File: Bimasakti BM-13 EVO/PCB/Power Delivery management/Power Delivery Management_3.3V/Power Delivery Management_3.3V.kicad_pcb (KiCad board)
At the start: 2 copper layers, 35 x 43 mm, 25 parts, among them J1 +12V In, J2 3.3V

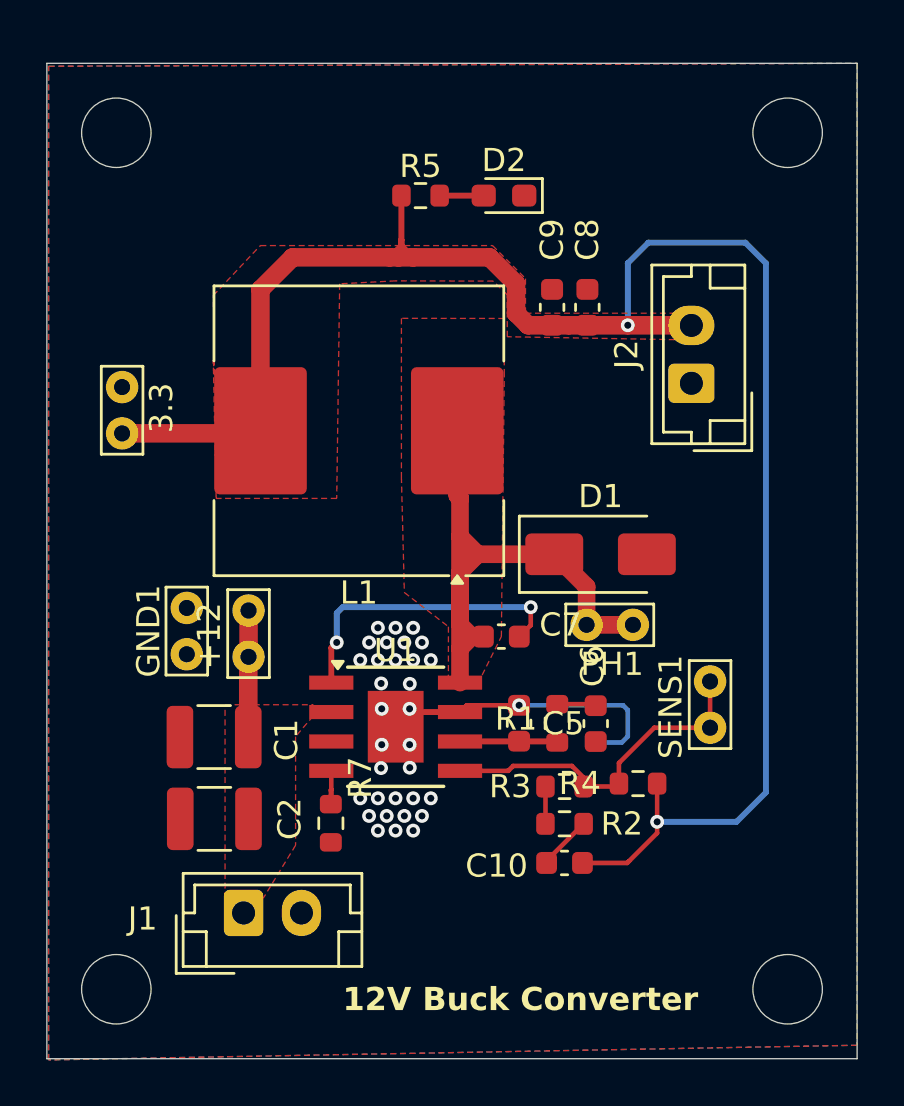
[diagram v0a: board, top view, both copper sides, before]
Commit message: pdm finishing tambah logo
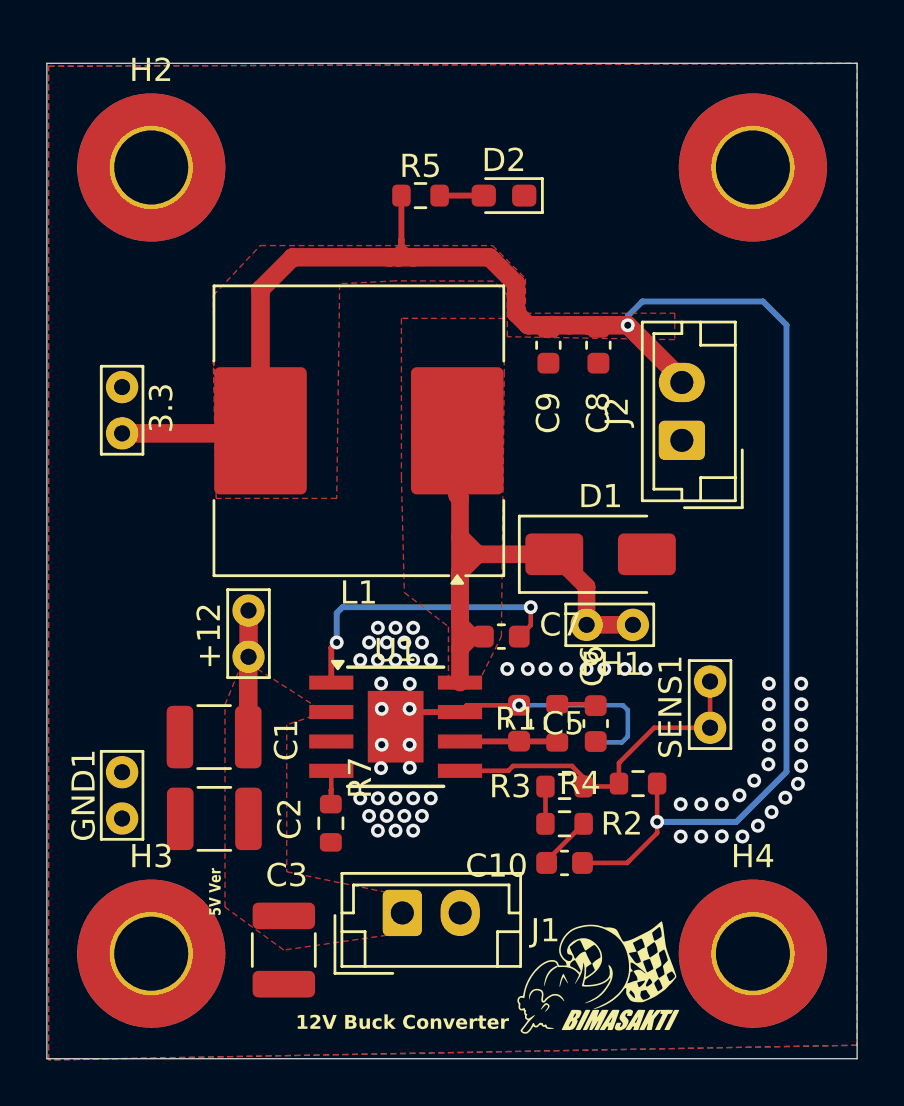
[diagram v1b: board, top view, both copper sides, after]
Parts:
- added C3: 22uF, Capacitor_SMD:C_1210_3225Metric, F.Cu at (51.1, 67.6)
- added G***: LOGO, logo:logo bimsak, F.Cu at (64.6, 68.8)
- added H1: MountingHole_Pad, MountingHole:MountingHole_3.2mm_M3_Pad_TopBottom, F.Cu at (71.3, 33.8)
- added H2: MountingHole_Pad, MountingHole:MountingHole_3.2mm_M3_Pad_TopBottom, F.Cu at (45.3, 33.8)
- added H3: MountingHole_Pad, MountingHole:MountingHole_3.2mm_M3_Pad_TopBottom, F.Cu at (45.3, 67.8)
- added H4: MountingHole_Pad, MountingHole:MountingHole_3.2mm_M3_Pad_TopBottom, F.Cu at (71.3, 67.8)
- D1: value 950mV 10A -> SS34
- R1: value 50k -> 5k
- moved GND1 7.63 mm to (44.1, 62.0)
- moved J1 6.86 mm to (56.2, 66.0)
- moved J2 2.50 mm to (68.2, 45.6)
- moved C8 1.71 mm to (64.6, 41.5), turned to -90 degrees
- moved C9 1.65 mm to (62.5, 41.5), turned to -90 degrees
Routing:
- net 3.3V: track 81.1 -> 78.1 mm
- net GND: vias 33 -> 64
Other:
- outline, holes or cut-outs redrawn
- board text added: "5V Ver"

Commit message: cicil assembly
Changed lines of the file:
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@@
 	)
 	(gr_text "5V Ver\n"
-		(at 48.387 66.167 90)
+		(at 51.27238 68.373138 90)
 		(layer "F.SilkS")
 		(effects
 			(font
-				(size 0.5 0.4)
-				(thickness 0.08)
+				(size 0.4 0.3)
+				(thickness 0.06)
 				(bold yes)
 			)
@@
 		(polygon
 			(pts
-				(xy 48.514 65.786) (xy 48.514 57.046385) (xy 49.149 55.499) (xy 49.911 55.499) (xy 49.911 55.499)
-				(xy 52.324 57.046385) (xy 52.324 57.531) (xy 51.181 57.912) (xy 51.181 64.262) (xy 55.499 65.151)
-				(xy 55.499 67.004252) (xy 51.054 67.642)
+				(xy 49.276 67.564) (xy 49.276 65.024) (xy 48.514 64.516) (xy 48.514 57.046385) (xy 49.149 55.499)
+				(xy 49.911 55.499) (xy 52.94547 57.077206) (xy 52.936392 57.658173) (xy 51.184761 58.542893) (xy 51.181 64.262)
+				(xy 55.499 65.151) (xy 55.499 67.004252) (xy 51.054 67.564)
 			)
 		)
@@
 		(layers "F.Cu" "B.Cu")
 		(hatch edge 0.5)
-		(connect_pads yes
+		(connect_pads
 			(clearance 0.381)
 		)
@@
 		(polygon
 			(pts
-				(xy 40.894 29.464) (xy 75.819 29.337) (xy 75.819 71.755) (xy 40.894 72.39)
+				(xy 40.894 29.464) (xy 75.819 29.337) (xy 75.819 72.136) (xy 40.894 72.39)
 			)
 		)

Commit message: ngecilin pdm
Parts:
- removed H1, H2, H3, H4: MountingHole_Pad, MountingHole:MountingHole_3.2mm_M3_Pad_TopBottom
- removed J1: +12V In, Connector_JST:JST_EH_B2B-EH-A_1x02_P2.50mm_Vertical
- removed J2: 3.3V, Connector_JST:JST_EH_B2B-EH-A_1x02_P2.50mm_Vertical
- added J3: Conn_01x10_Socket, Connector_PinHeader_2.54mm:PinHeader_1x10_P2.54mm_Vertical, B.Cu at (47.1, 68.4)
- added J4: Conn_01x10_Socket, Connector_PinHeader_2.54mm:PinHeader_1x10_P2.54mm_Vertical, B.Cu at (47.1, 43.9)
- L1: footprint Inductor_SMD:L_Coilcraft_MSS1278T-XXX -> Inductor_SMD:L_Changjiang_FNR5020S
- R5: value 220 -> 2k
- moved G*** 18.4 mm to (71.0, 51.6), turned to 90 degrees
- moved GND1 15.0 mm to (48.0, 47.5), turned to 180 degrees
- moved C8 14.5 mm to (51.6, 47.9), turned to 90 degrees
- moved C9 14.1 mm to (49.9, 47.9), turned to 90 degrees
- moved D2 13.2 mm to (64.9, 47.5)
- moved R5 12.9 mm to (62.5, 46.7), turned to -90 degrees
- moved 3.3 10.0 mm to (46.9, 55.0)
- moved L1 4.01 mm to (55.5, 49.0)
- moved C3 3.82 mm to (48.0, 65.3), turned to 180 degrees
- moved R7 0.13 mm to (53.1, 62.3)
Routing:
- net 3.3V: track 78.1 -> 61.5 mm
- net GND: track 14.9 -> 7.43 mm, vias 64 -> 82
- net PH: track 25.8 -> 23.0 mm
- net +12V: track 5.47 -> 8.01 mm
- net Net-(U1-SS): track 1.68 -> 2.49 mm
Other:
- board size 35 x 43 mm -> 30 x 30 mm
- board text added: "12VIN"
- board text added: "GND"
- board text added: "VOUT"
- board text added: "semoga <10mvVpp"

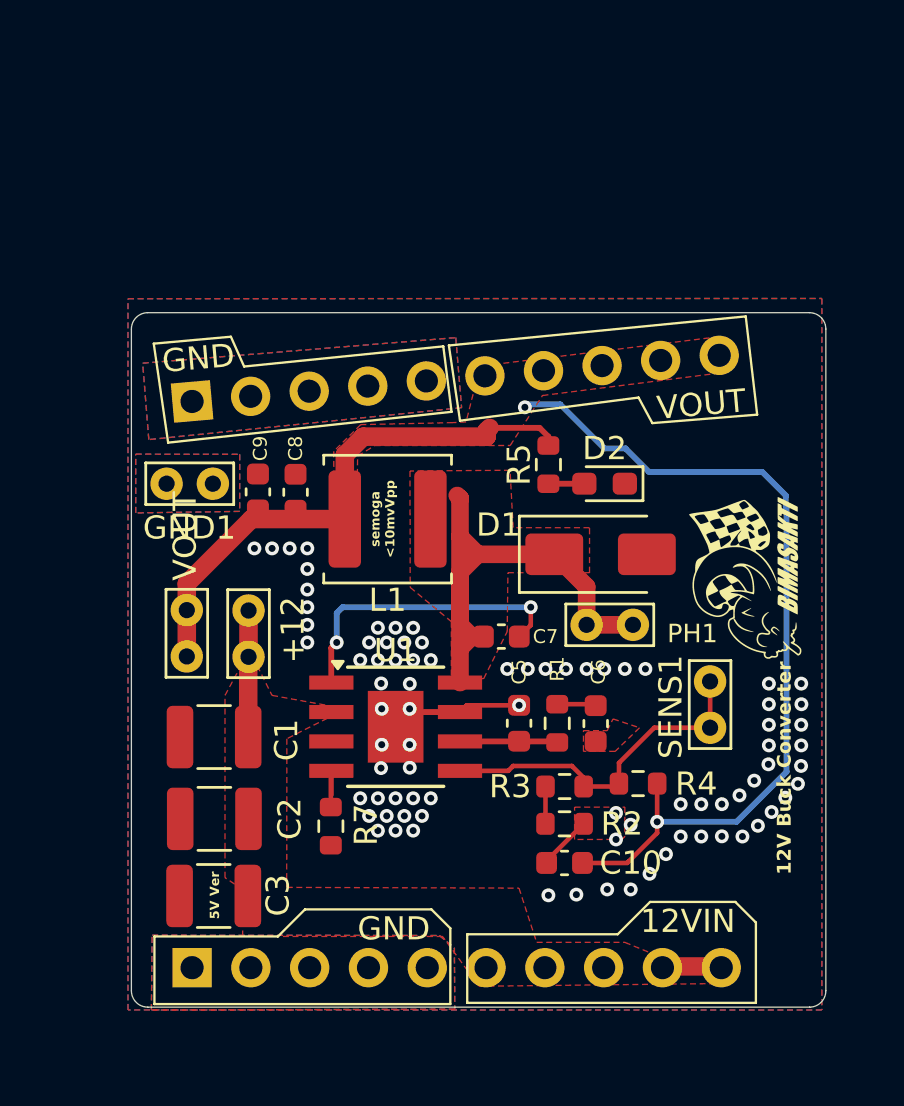
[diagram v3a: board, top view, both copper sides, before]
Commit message: buat placeholder baru dan ganti konektor
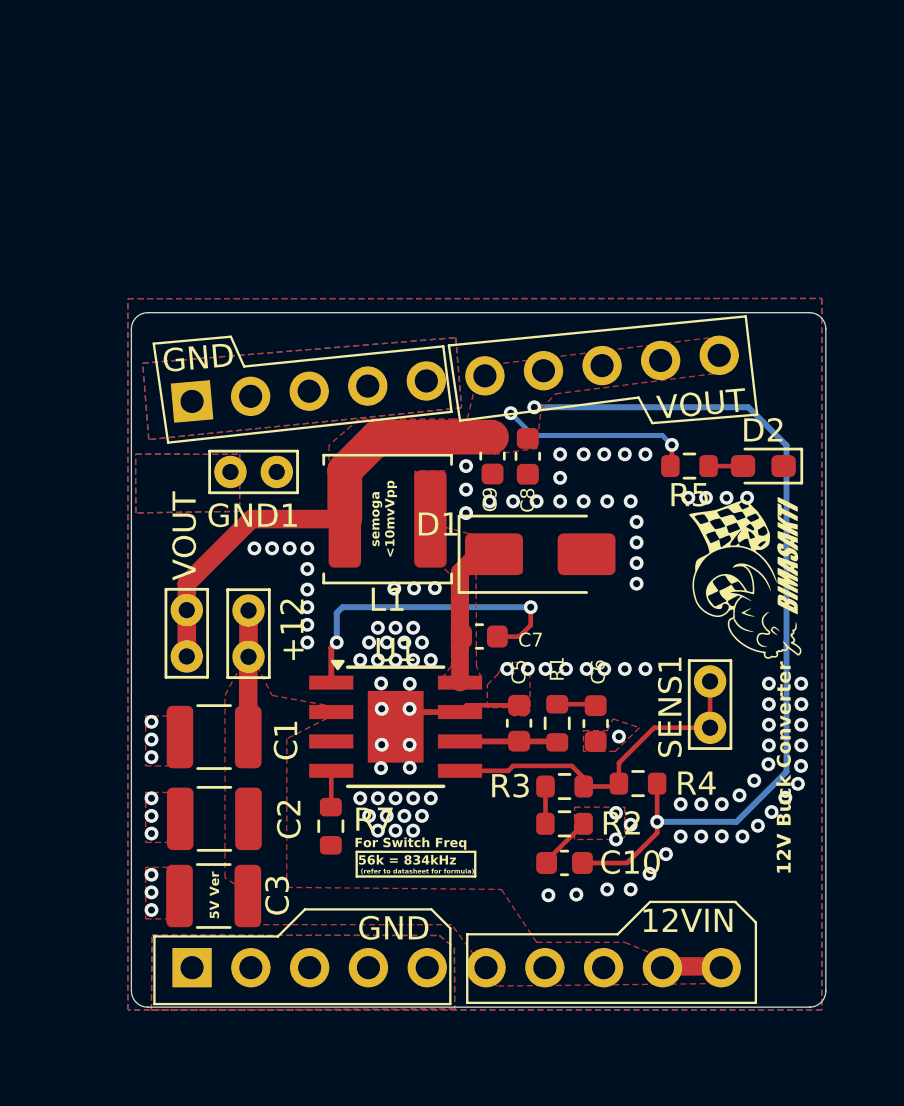
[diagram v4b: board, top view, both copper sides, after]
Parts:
- removed PH1: TestPoint, TestPoint:TestPoint_Bridge_Pitch2.0mm_Drill0.7mm
- R5: value 2k -> 500
- moved C9 10.3 mm to (60.1, 46.3), turned to -90 degrees
- moved C8 10.2 mm to (61.6, 46.3), turned to -90 degrees
- moved D2 6.90 mm to (71.8, 46.7)
- moved R5 6.10 mm to (68.6, 46.7), turned to 0 degrees
- moved GND1 2.81 mm to (50.7, 47.0)
- moved D1 2.60 mm to (62.1, 50.5)
- moved C7 0.95 mm to (59.5, 54.1)
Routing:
- net PH: track 23.0 -> 8.52 mm
- net 3.3V: track 61.5 -> 66.7 mm, vias 2 -> 4
- net Net-(U1-SS): track 2.49 -> 1.60 mm
- net BOOT: track 13.1 -> 13.9 mm
- net GND: vias 82 -> 118
- added copper zone on In1.Cu, net GND
- added copper zone on In2.Cu, net GND
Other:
- copper layers 2 -> 4
- board text added: "(refer to datasheet for formula)"
- board text added: "56k = 834kHz"
- board text added: "For Switch Freq"
